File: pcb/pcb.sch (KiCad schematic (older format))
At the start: 34 parts, among them J1 Conn_02x08_Odd_Even, J2 B2B-PH-K-S_LF__SN_, J3 USB_C_Receptacle, Q1 MMUN2211LT1G, SW1 SW_SPST, U1 TPS61090, U2 MCP73871-1AA

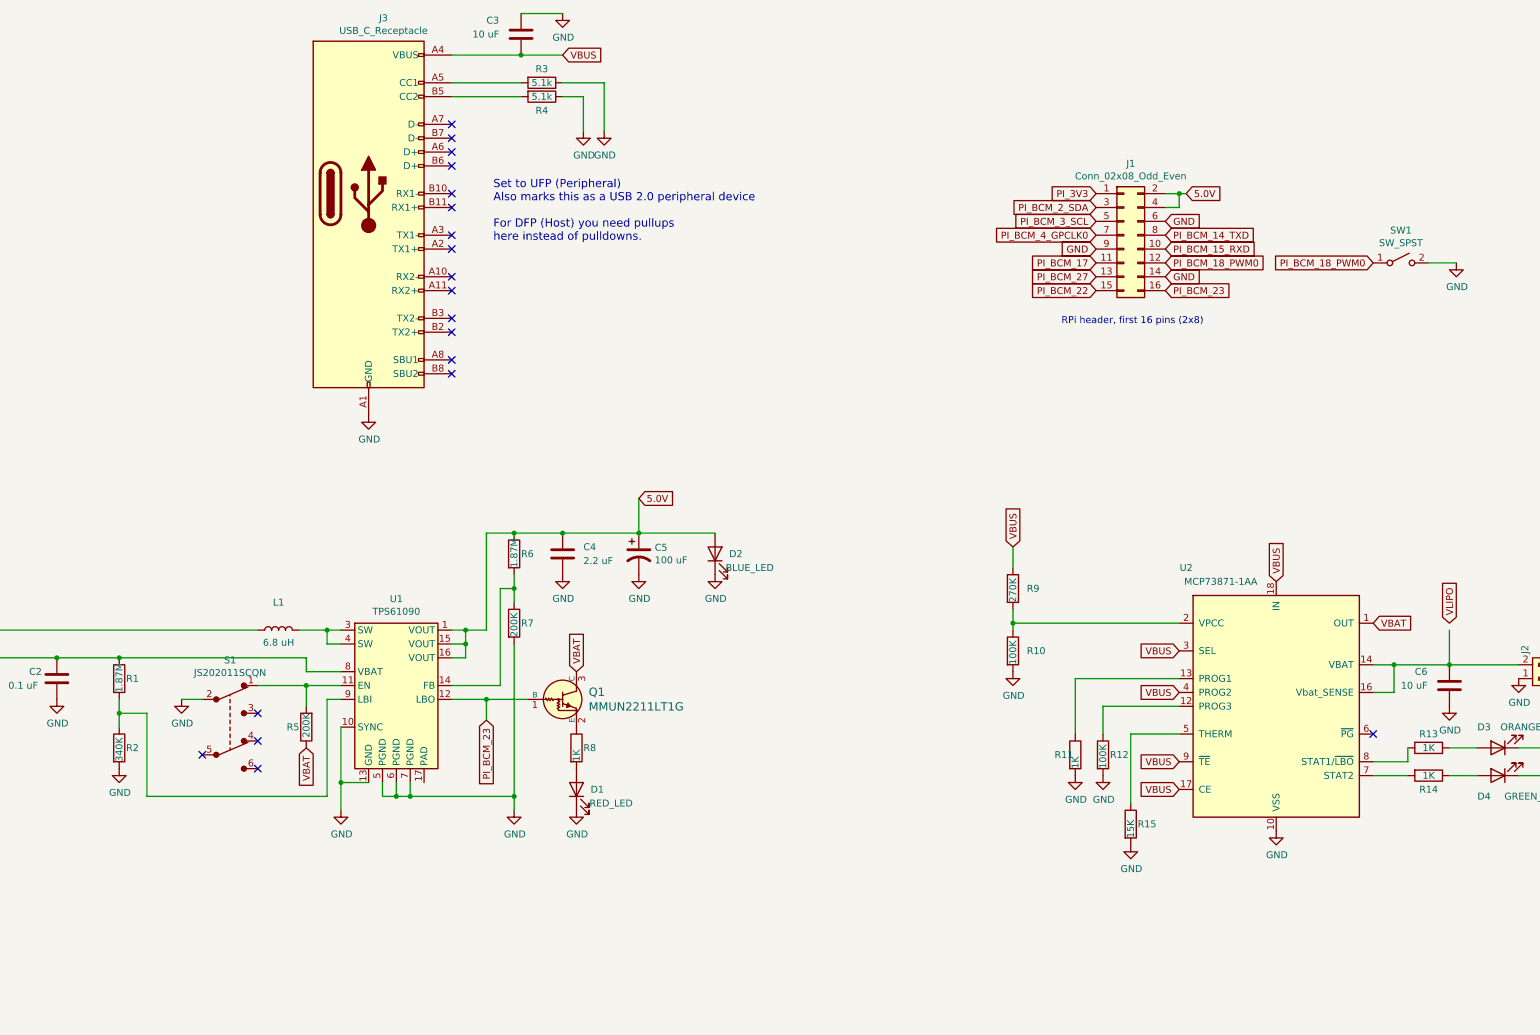
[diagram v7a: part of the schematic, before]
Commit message: updated cuts and placements, all 0805 SMD
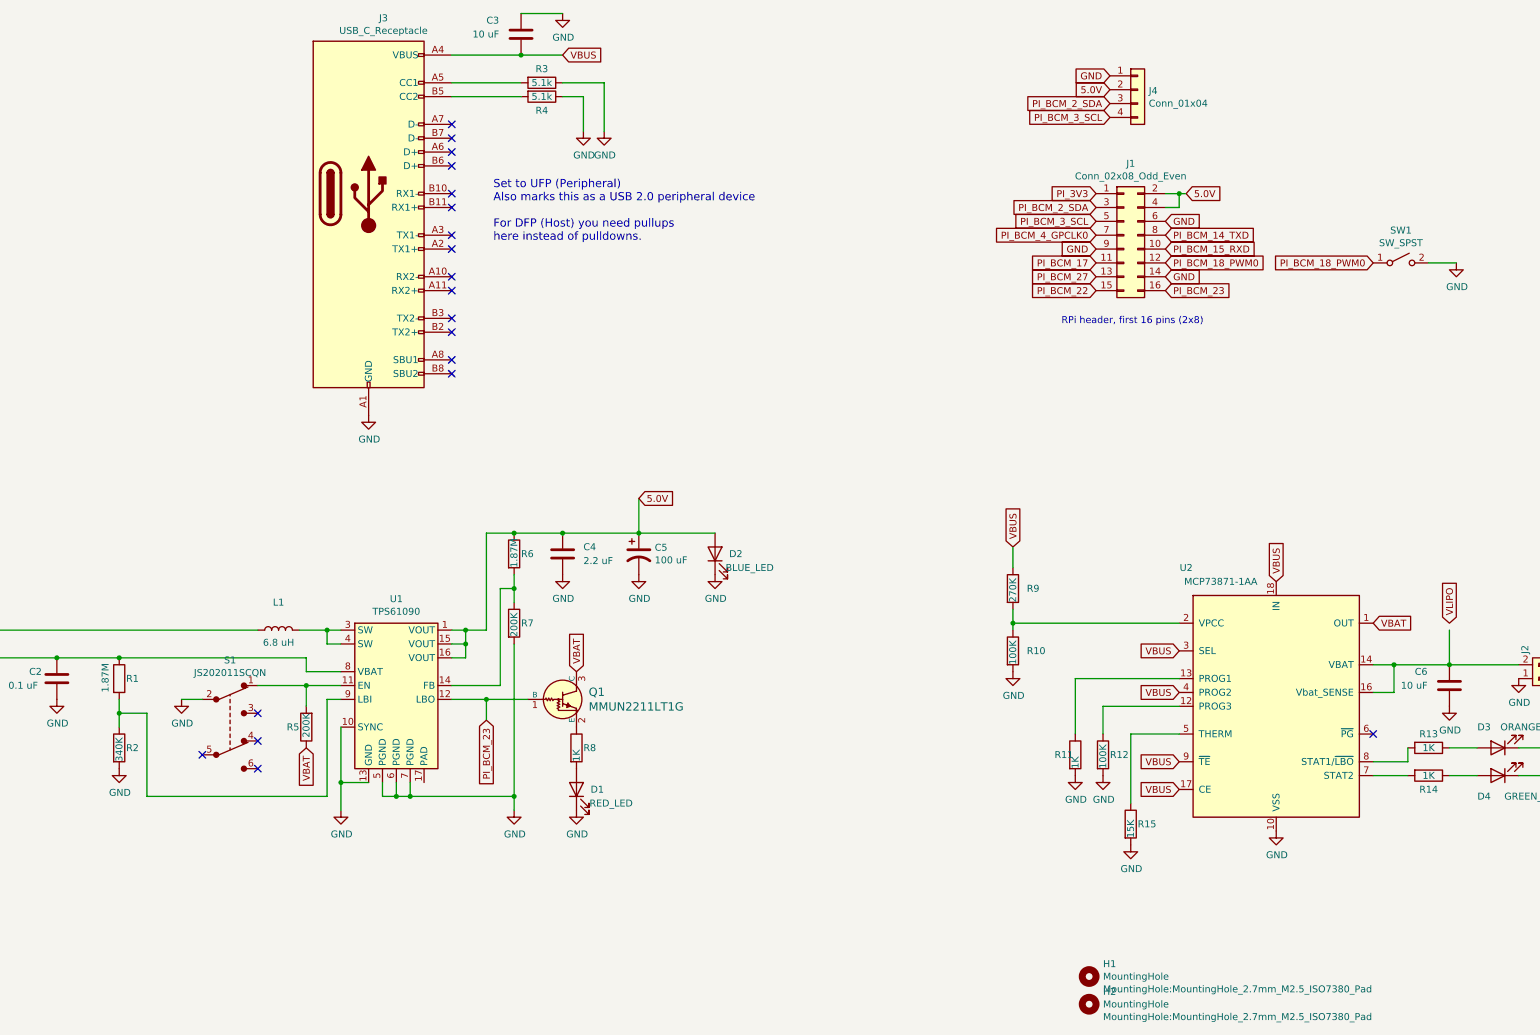
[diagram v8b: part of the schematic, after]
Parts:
- added H1, H2: MountingHole, MountingHole:MountingHole_2.7mm_M2.5_ISO7380_Pad, symbol Mechanical:MountingHole
- added J4: Conn_01x04, Connector_PinSocket_2.54mm:PinSocket_1x04_P2.54mm_Vertical, symbol Connector_Generic:Conn_01x04
- C2: footprint Capacitor_SMD:C_01005_0402Metric -> Capacitor_SMD:C_0805_2012Metric
- C4: footprint Capacitor_SMD:C_0201_0603Metric -> Capacitor_SMD:C_0805_2012Metric
- C5: footprint Capacitor_SMD:C_1206_3216Metric -> Capacitor_SMD:C_0805_2012Metric
- J1: footprint Connector_PinHeader_2.54mm:PinHeader_2x08_P2.54mm_Vertical -> Connector_PinSocket_2.54mm:PinSocket_2x08_P2.54mm_Vertical
- R1, R10, R11, R12, R13, R14, R15, R2, R3, R4, R5, R6, R7, R8: footprint Resistor_SMD:R_0402_1005Metric -> Resistor_SMD:R_0805_2012Metric
- R9: footprint Resistor_SMD:R_0201_0603Metric -> Resistor_SMD:R_0805_2012Metric
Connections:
- net 5.0V: now also J4.2 (Pin_2)
- net GND: now also J4.1 (Pin_1)
- net PI_BCM_2_SDA: now also J4.3 (Pin_3)
- net PI_BCM_3_SCL: now also J4.4 (Pin_4)
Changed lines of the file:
@@
 F 0 "J1" H 10750 4467 50  0000 C CNN
 F 1 "Conn_02x08_Odd_Even" H 10750 4376 50  0000 C CNN
-F 2 "Connector_PinHeader_2.54mm:PinHeader_2x08_P2.54mm_Vertical" H 10700 3950 50  0001 C CNN
+F 2 "Connector_PinSocket_2.54mm:PinSocket_2x08_P2.54mm_Vertical" H 10700 3950 50  0001 C CNN
 F 3 "~" H 10700 3950 50  0001 C CNN
 	1    10700 3950
@@
 F 0 "R3" V 6400 2850 50  0000 C CNN
 F 1 "5.1k" V 6500 2850 50  0000 C CNN
-F 2 "Resistor_SMD:R_0402_1005Metric" V 6430 2850 50  0001 C CNN
+F 2 "Resistor_SMD:R_0805_2012Metric" V 6430 2850 50  0001 C CNN
 F 3 "https://www.digikey.com/product-detail/en/yageo/RC0402FR-075K1L/311-5-10KLRCT-ND/729571" H 6500 2850 50  0001 C CNN
 	1    6500 2850
@@
 F 0 "R4" V 6600 2950 50  0000 C CNN
 F 1 "5.1k" V 6500 2950 50  0000 C CNN
-F 2 "Resistor_SMD:R_0402_1005Metric" V 6430 2950 50  0001 C CNN
+F 2 "Resistor_SMD:R_0805_2012Metric" V 6430 2950 50  0001 C CNN
 F 3 "~" H 6500 2950 50  0001 C CNN
 	1    6500 2950
@@
 F 0 "R9" H 10000 6500 50  0000 L CNN
 F 1 "270K" V 9900 6400 50  0000 L CNN
-F 2 "Resistor_SMD:R_0201_0603Metric" V 9830 6500 50  0001 C CNN
+F 2 "Resistor_SMD:R_0805_2012Metric" V 9830 6500 50  0001 C CNN
 F 3 "https://www.digikey.com/product-detail/en/yageo/RC0201FR-07270KL/YAG2548CT-ND/5281412" H 9900 6500 50  0001 C CNN
 	1    9900 6500
@@
 F 0 "R10" H 10000 6950 50  0000 L CNN
 F 1 "100K" V 9900 6850 50  0000 L CNN
-F 2 "Resistor_SMD:R_0402_1005Metric" V 9830 6950 50  0001 C CNN
+F 2 "Resistor_SMD:R_0805_2012Metric" V 9830 6950 50  0001 C CNN
 F 3 "~" H 9900 6950 50  0001 C CNN
 	1    9900 6950
@@
 F 0 "R12" H 10600 7700 50  0000 L CNN
 F 1 "100K" V 10550 7600 50  0000 L CNN
-F 2 "Resistor_SMD:R_0402_1005Metric" V 10480 7700 50  0001 C CNN
+F 2 "Resistor_SMD:R_0805_2012Metric" V 10480 7700 50  0001 C CNN
 F 3 "https://www.digikey.com/product-detail/en/yageo/RC0402FR-07100KL/311-100KLRCT-ND/729473" H 10550 7700 50  0001 C CNN
 	1    10550 7700
@@
 F 0 "R11" H 10200 7700 50  0000 L CNN
 F 1 "1K" V 10350 7600 50  0000 L CNN
-F 2 "Resistor_SMD:R_0402_1005Metric" V 10280 7700 50  0001 C CNN
+F 2 "Resistor_SMD:R_0805_2012Metric" V 10280 7700 50  0001 C CNN
 F 3 "~" H 10350 7700 50  0001 C CNN
 	1    10350 7700
@@
 F 0 "R13" V 12800 7650 50  0000 C CNN
 F 1 "1K" V 12900 7650 50  0000 C CNN
-F 2 "Resistor_SMD:R_0402_1005Metric" V 12830 7650 50  0001 C CNN
+F 2 "Resistor_SMD:R_0805_2012Metric" V 12830 7650 50  0001 C CNN
 F 3 "https://www.digikey.com/product-detail/en/yageo/RC0402FR-071KL/311-1-00KLRCT-ND/729460" H 12900 7650 50  0001 C CNN
 	1    12900 7650
@@
 F 0 "R14" V 13000 7850 50  0000 C CNN
 F 1 "1K" V 12900 7850 50  0000 C CNN
-F 2 "Resistor_SMD:R_0402_1005Metric" V 12830 7850 50  0001 C CNN
+F 2 "Resistor_SMD:R_0805_2012Metric" V 12830 7850 50  0001 C CNN
 F 3 "~" H 12900 7850 50  0001 C CNN
 	1    12900 7850
@@
 F 0 "R5" H 4850 7500 50  0000 L CNN
 F 1 "200K" V 4800 7400 50  0000 L CNN
-F 2 "Resistor_SMD:R_0402_1005Metric" V 4730 7500 50  0001 C CNN
+F 2 "Resistor_SMD:R_0805_2012Metric" V 4730 7500 50  0001 C CNN
 F 3 "https://www.digikey.com/product-detail/en/yageo/RT0402BRD07200KL/YAG4202CT-ND/6616358" H 4800 7500 50  0001 C CNN
 	1    4800 7500
@@
 F 0 "R8" H 6800 7650 50  0000 L CNN
 F 1 "1K" V 6750 7550 50  0000 L CNN
-F 2 "Resistor_SMD:R_0402_1005Metric" V 6680 7650 50  0001 C CNN
+F 2 "Resistor_SMD:R_0805_2012Metric" V 6680 7650 50  0001 C CNN
 F 3 "~" H 6750 7650 50  0001 C CNN
 	1    6750 7650
@@
 F 0 "R6" H 6350 6250 50  0000 L CNN
 F 1 "1.87M" V 6300 6150 50  0000 L CNN
-F 2 "Resistor_SMD:R_0402_1005Metric" V 6230 6250 50  0001 C CNN
+F 2 "Resistor_SMD:R_0805_2012Metric" V 6230 6250 50  0001 C CNN
 F 3 "~" H 6300 6250 50  0001 C CNN
 	1    6300 6250
@@
 F 0 "R7" H 6350 6750 50  0000 L CNN
 F 1 "200K" V 6300 6650 50  0000 L CNN
-F 2 "Resistor_SMD:R_0402_1005Metric" V 6230 6750 50  0001 C CNN
+F 2 "Resistor_SMD:R_0805_2012Metric" V 6230 6750 50  0001 C CNN
 F 3 "~" H 6300 6750 50  0001 C CNN
 	1    6300 6750
@@
 F 0 "C4" H 6800 6300 50  0000 L CNN
 F 1 "2.2 uF" H 6800 6200 50  0000 L CNN
-F 2 "Capacitor_SMD:C_0201_0603Metric" H 6688 6100 50  0001 C CNN
+F 2 "Capacitor_SMD:C_0805_2012Metric" H 6688 6100 50  0001 C CNN
 F 3 "https://www.digikey.com/product-detail/en/C0603C225M9PAC7867/399-13137-1-ND/5879291/?itemSeq=336152622" H 6650 6250 50  0001 C CNN
 	1    6650 6250
@@
 F 0 "C5" H 7315 6296 50  0000 L CNN
 F 1 "100 uF" H 7315 6205 50  0000 L CNN
-F 2 "Capacitor_SMD:C_1206_3216Metric" H 7200 6250 50  0001 C CNN
+F 2 "Capacitor_SMD:C_0805_2012Metric" H 7200 6250 50  0001 C CNN
 F 3 "https://www.digikey.com/product-detail/en/kemet/C1206C107M9PACTU/399-5620-1-ND/2057834" H 7200 6250 50  0001 C CNN
 	1    7200 6250
@@
 F 0 "C2" H 2800 7200 50  0000 L CNN
 F 1 "0.1 uF" H 2650 7100 50  0000 L CNN
-F 2 "Capacitor_SMD:C_01005_0402Metric" H 3038 7000 50  0001 C CNN
+F 2 "Capacitor_SMD:C_0805_2012Metric" H 3038 7000 50  0001 C CNN
 F 3 "~" H 3000 7150 50  0001 C CNN
 	1    3000 7150
@@
 P 3450 7150
 F 0 "R1" H 3500 7150 50  0000 L CNN
-F 1 "1.87M" V 3450 7050 50  0000 L CNN
-F 2 "Resistor_SMD:R_0402_1005Metric" V 3380 7150 50  0001 C CNN
+F 1 "1.87M" V 3350 7050 50  0000 L CNN
+F 2 "Resistor_SMD:R_0805_2012Metric" V 3380 7150 50  0001 C CNN
 F 3 "https://www.digikey.com/product-detail/en/stackpole-electronics-inc/RMCF0402FT1M87/RMCF0402FT1M87CT-ND/7790634" H 3450 7150 50  0001 C CNN
 	1    3450 7150
@@
 F 0 "R2" H 3500 7650 50  0000 L CNN
 F 1 "340K" V 3450 7550 50  0000 L CNN
-F 2 "Resistor_SMD:R_0402_1005Metric" V 3380 7650 50  0001 C CNN
+F 2 "Resistor_SMD:R_0805_2012Metric" V 3380 7650 50  0001 C CNN
 F 3 "https://www.digikey.com/product-detail/en/panasonic-electronic-components/ERJ-2RKF3403X/P340KLCT-ND/194356" H 3450 7650 50  0001 C CNN
 	1    3450 7650
@@
 F 0 "R15" H 10800 8200 50  0000 L CNN
 F 1 "15K" V 10750 8100 50  0000 L CNN
-F 2 "Resistor_SMD:R_0402_1005Metric" V 10680 8200 50  0001 C CNN
+F 2 "Resistor_SMD:R_0805_2012Metric" V 10680 8200 50  0001 C CNN
 F 3 "https://www.digikey.com/product-detail/en/yageo/RT0402BRD0715KL/YAG2302CT-ND/5252416" H 10750 8200 50  0001 C CNN
 	1    10750 8200
@@
 	1    0    0    -1
 $EndComp
+$Comp
+L Connector_Generic:Conn_01x04 J4
+U 1 1 5F46CA4B
+P 10800 2900
+F 0 "J4" H 10880 2892 50  0000 L CNN
+F 1 "Conn_01x04" H 10880 2801 50  0000 L CNN
+F 2 "Connector_PinSocket_2.54mm:PinSocket_1x04_P2.54mm_Vertical" H 10800 2900 50  0001 C CNN
+F 3 "~" H 10800 2900 50  0001 C CNN
+	1    10800 2900
+	1    0    0    -1
+$EndComp
+Text GLabel 10600 2900 0    50   Input ~ 0
+5.0V
+Text GLabel 10600 3000 0    50   Input ~ 0
+PI_BCM_2_SDA
+Text GLabel 10600 3100 0    50   Input ~ 0
+PI_BCM_3_SCL
+Text GLabel 10600 2800 0    50   Input ~ 0
+GND
+$Comp
+L Mechanical:MountingHole H1
+U 1 1 5F479AFB
+P 10450 9300
+F 0 "H1" H 10550 9391 50  0000 L CNN
+F 1 "MountingHole" H 10550 9300 50  0000 L CNN
+F 2 "MountingHole:MountingHole_2.7mm_M2.5_ISO7380_Pad" H 10550 9209 50  0000 L CNN
+F 3 "~" H 10450 9300 50  0001 C CNN
+	1    10450 9300
+	1    0    0    -1
+$EndComp
+$Comp
+L Mechanical:MountingHole H2
+U 1 1 5F47B4E8
+P 10450 9500
+F 0 "H2" H 10550 9591 50  0000 L CNN
+F 1 "MountingHole" H 10550 9500 50  0000 L CNN
+F 2 "MountingHole:MountingHole_2.7mm_M2.5_ISO7380_Pad" H 10550 9409 50  0000 L CNN
+F 3 "~" H 10450 9500 50  0001 C CNN
+	1    10450 9500
+	1    0    0    -1
+$EndComp
